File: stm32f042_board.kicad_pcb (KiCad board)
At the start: 4 copper layers, 40.6 x 18.8 mm, 23 parts, among them J1 Conn_01x12_Female, J2 Conn_01x12_Female, J3 USB_B_Micro, J5 JTAG/SWD, U1 STM32F042F6Px, U2 MCP1802, U3 USBLC6-2SC6

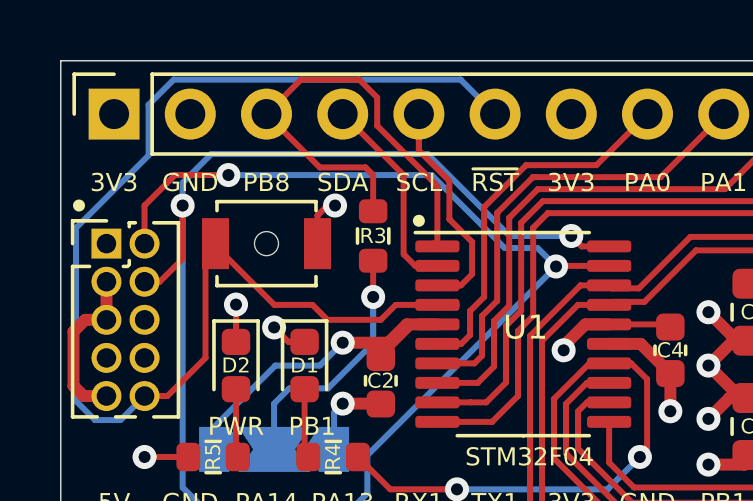
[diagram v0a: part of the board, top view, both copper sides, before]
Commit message: move a via to reconnect the isolated 3V3 and GND pours (pins 1 and 2)
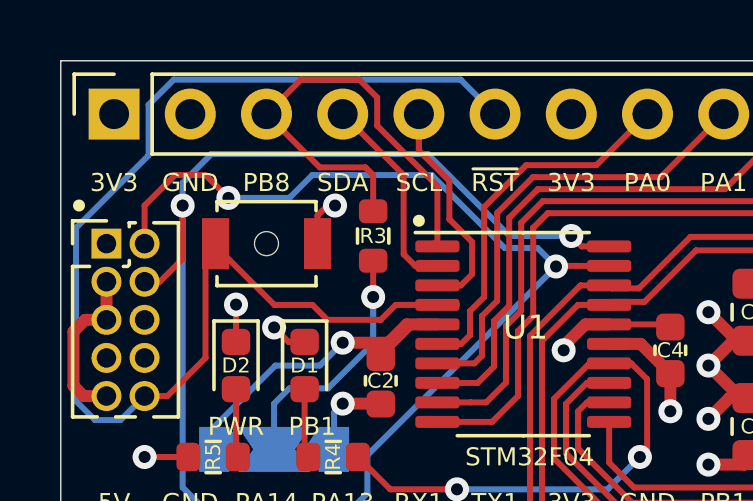
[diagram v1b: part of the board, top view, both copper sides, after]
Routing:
- net SWDIO: track 31.7 -> 32.3 mm

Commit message: oops. connect 3v3 on jtag header.
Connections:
- J5 pad 1: Net-(J5-Pad1) -> +3V3

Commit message: make smaller
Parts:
- moved FB1 9.71 mm to (170.4, 67.4), turned to 90 degrees
- moved C9 9.43 mm to (172.5, 67.4), turned to 270 degrees
- moved C10 8.93 mm to (168.4, 67.4), turned to 90 degrees
- moved U2 4.46 mm to (164.2, 69.4)
- moved U3 3.81 mm to (170.4, 63.4)
- moved J3 3.02 mm to (176.3, 64.1)
- moved C3 2.73 mm to (164.2, 66.6), turned to 0 degrees
- moved C11 2.52 mm to (175.4, 71.2)
- moved C1 1.73 mm to (169.3, 70.4), turned to 0 degrees
- moved R5 0.95 mm to (147.3, 70.4)
- moved C5 0.90 mm to (164.2, 64.6), turned to 0 degrees
- moved J5 0.76 mm to (142.7, 64.0)
- moved D2 0.25 mm to (147.3, 67.3)
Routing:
- net USB_VBUS: track 17.6 -> 10.2 mm
- net GND: track 44.9 -> 40.9 mm, vias 14 -> 9
- net USB+: track 28.7 -> 24.9 mm
- net USB-: track 26.2 -> 22.5 mm
- net NRST: track 42.5 -> 45.7 mm
- net +3V3: track 30.8 -> 28.5 mm, vias 6 -> 3
- net USB_D-: track 2.49 -> 4.38 mm
- net USB_D+: track 2.55 -> 4.43 mm
- net SWCLK: track 33.4 -> 34.3 mm
- net SWDIO: track 32.3 -> 33.1 mm
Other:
- board size 40.6 x 18.8 mm -> 37.8 x 18.8 mm

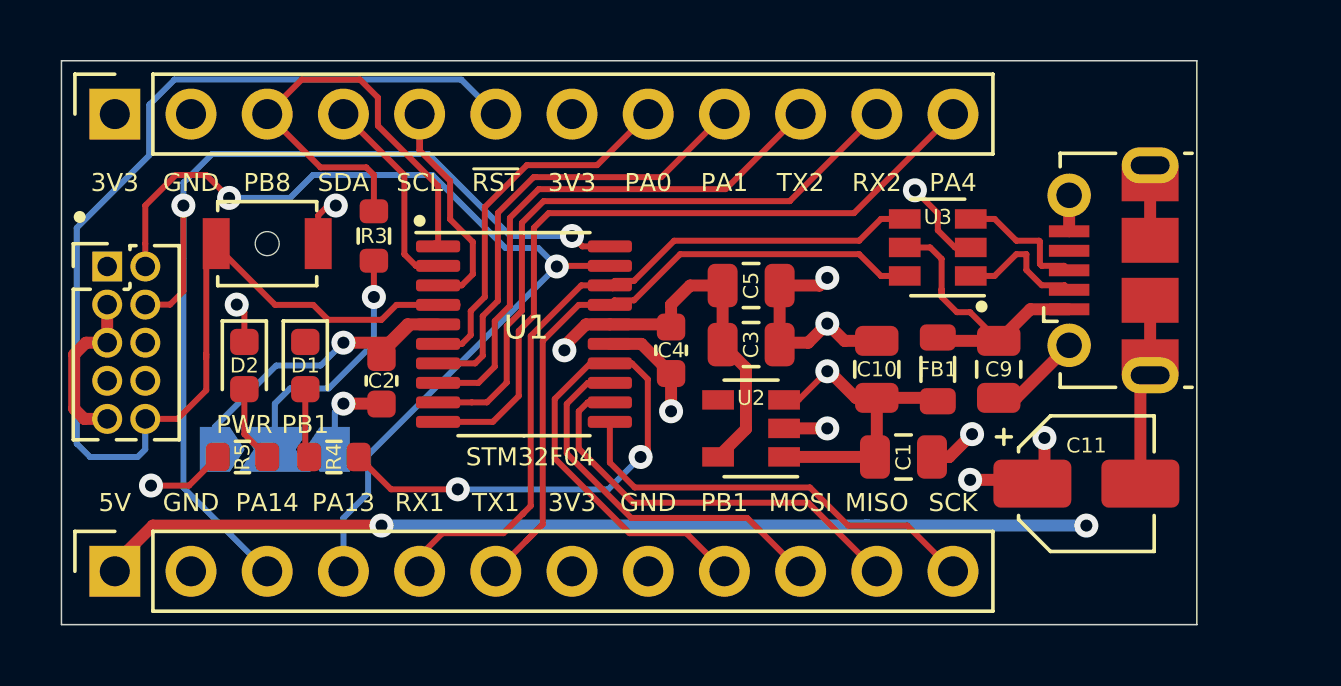
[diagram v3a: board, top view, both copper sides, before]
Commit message: Fix user LED ground; Update kicad version
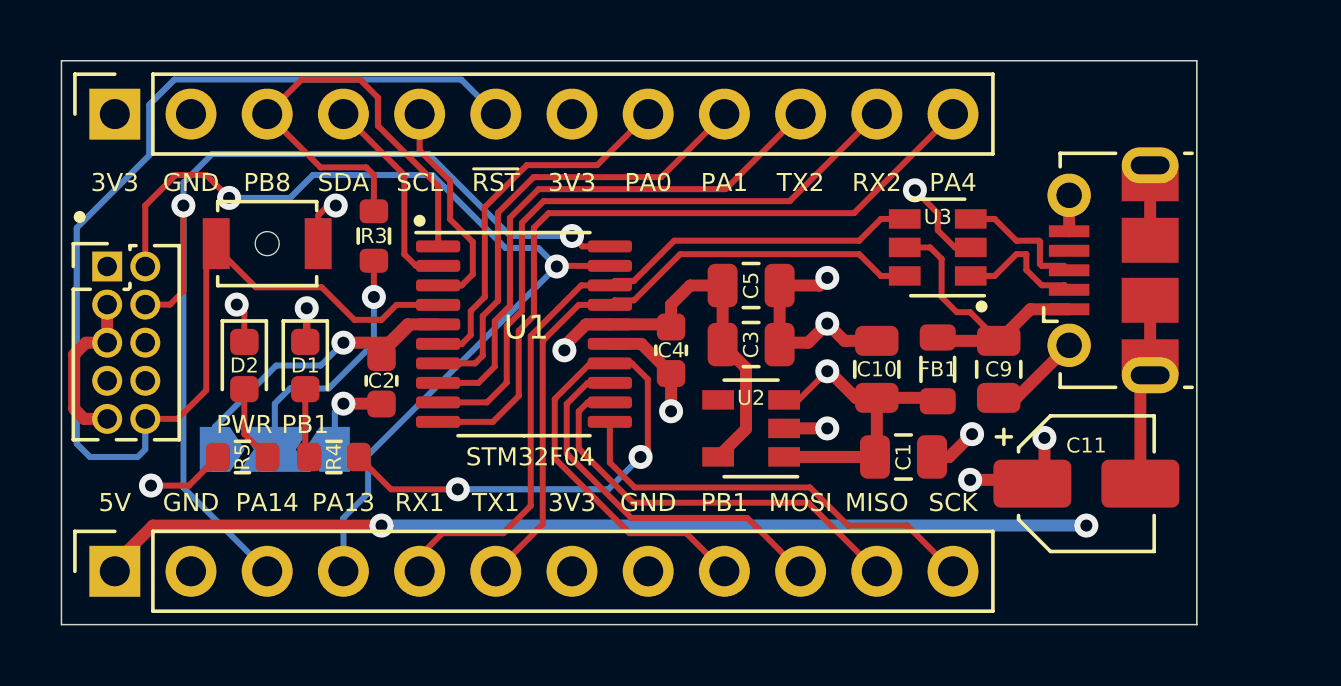
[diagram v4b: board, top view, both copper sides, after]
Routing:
- net NRST: track 45.7 -> 44.5 mm
- net +3V3: track 28.5 -> 27.7 mm
- net GND: track 40.9 -> 41.6 mm, vias 9 -> 10
- net PA1: track 16.1 -> 15.5 mm
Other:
- net class Default removed
- board text added: "~{RST}"
- board text removed: "~RST"

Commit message: Add identifying text on rear silkscreen
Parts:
- added G***: LOGO, LOGO, B.Cu at (176.6, 70.4)
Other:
- board text added: "STM32F042 breakout, v2 Jed Parsons github.com/jedp/"

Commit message: Bug fixes
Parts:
- added R1: 0k, Resistor_SMD:R_0603_1608Metric, F.Cu at (176.7, 58.6)
- moved C4 0.55 mm to (161.5, 67.3)
- moved C3 0.19 mm to (164.4, 66.6)
- moved C5 0.19 mm to (164.4, 64.6)
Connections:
- J3 pad 4: Net-(J3-Pad4) -> unconnected-(J3-Pad4)
- J3 pad 6: GND -> Net-(J3-Pad6)
- J5 pad 6: Net-(J5-Pad6) -> unconnected-(J5-Pad6)
- J5 pad 7: Net-(J5-Pad7) -> unconnected-(J5-Pad7)
- J5 pad 8: Net-(J5-Pad8) -> unconnected-(J5-Pad8)
- U2 pad 4: Net-(U2-Pad4) -> unconnected-(U2-Pad4)
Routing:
- net Net-(J3-Pad6): track 0.00 -> 13.8 mm
- net VBUS: track 49.2 -> 52.2 mm, vias 5 -> 7
- net GND: track 41.6 -> 38.9 mm, vias 10 -> 15
- net +3V3: track 27.7 -> 26.2 mm, vias 3 -> 5
- net USB+: track 24.7 -> 23.3 mm
- net USB-: track 22.0 -> 22.7 mm
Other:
- outline, holes or cut-outs redrawn
- board text added: "STM32F042 breakout, v3 Jed Parsons github.com/jedp/"
- board text added: "VBUS 5V"
- board text removed: "STM32F042 breakout, v2 Jed Parsons github.com/jedp/"

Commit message: Migrate to KiCad 7
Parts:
- moved G*** 12.5 mm to (164.3, 68.6), turned to -90 degrees
- moved C4 0.66 mm to (161.4, 66.7)
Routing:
- net +3V3: track 26.2 -> 27.8 mm, vias 5 -> 4
- net SWDIO: track 32.9 -> 33.5 mm
- net GND: track 38.9 -> 38.4 mm

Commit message: Revert "Migrate to KiCad 7"
This reverts commit a80925b01a00ac2b6e233b577ff1a59522959ffa.

- Footprints and some other things don't seem to work right yet
- OSHPark not v7 compatible yet.
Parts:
- moved G*** 12.5 mm to (176.6, 70.4), turned to 0 degrees
- moved C4 0.66 mm to (161.5, 67.3)
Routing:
- net +3V3: track 27.8 -> 26.2 mm, vias 4 -> 5
- net SWDIO: track 33.5 -> 32.9 mm
- net GND: track 38.4 -> 38.9 mm
